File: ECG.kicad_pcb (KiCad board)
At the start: 4 copper layers, 60 x 60 mm, 95 parts, among them J1 SJ-3566AN, J2 Conn_01x02_Male, J3 Conn_01x08_Male, J4 Conn_01x02_Male, J5 Conn_ARM_JTAG_SWD_10, Q1 BC858, Q2 Q_NMOS_DGS, U1 ADR4525, U2 LTC3531, U3 INA333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

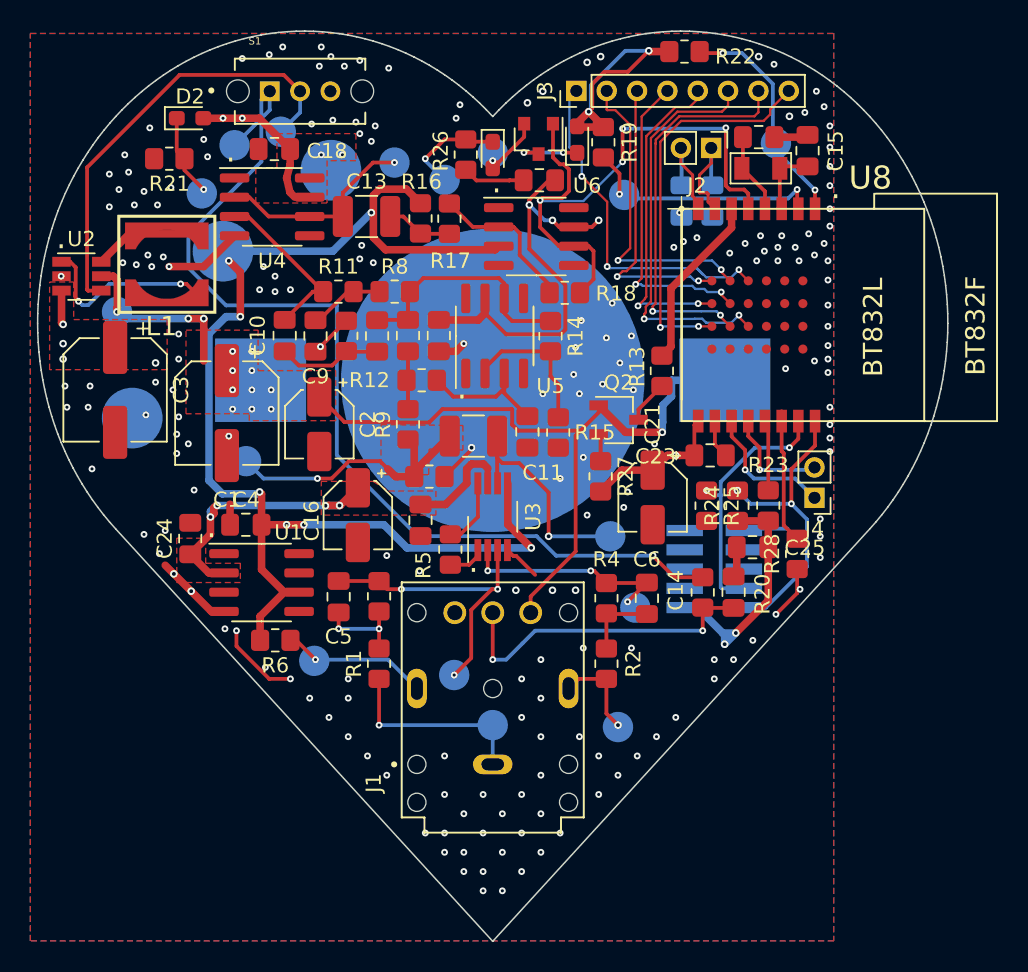
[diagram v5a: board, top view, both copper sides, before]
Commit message: Updated silk screen
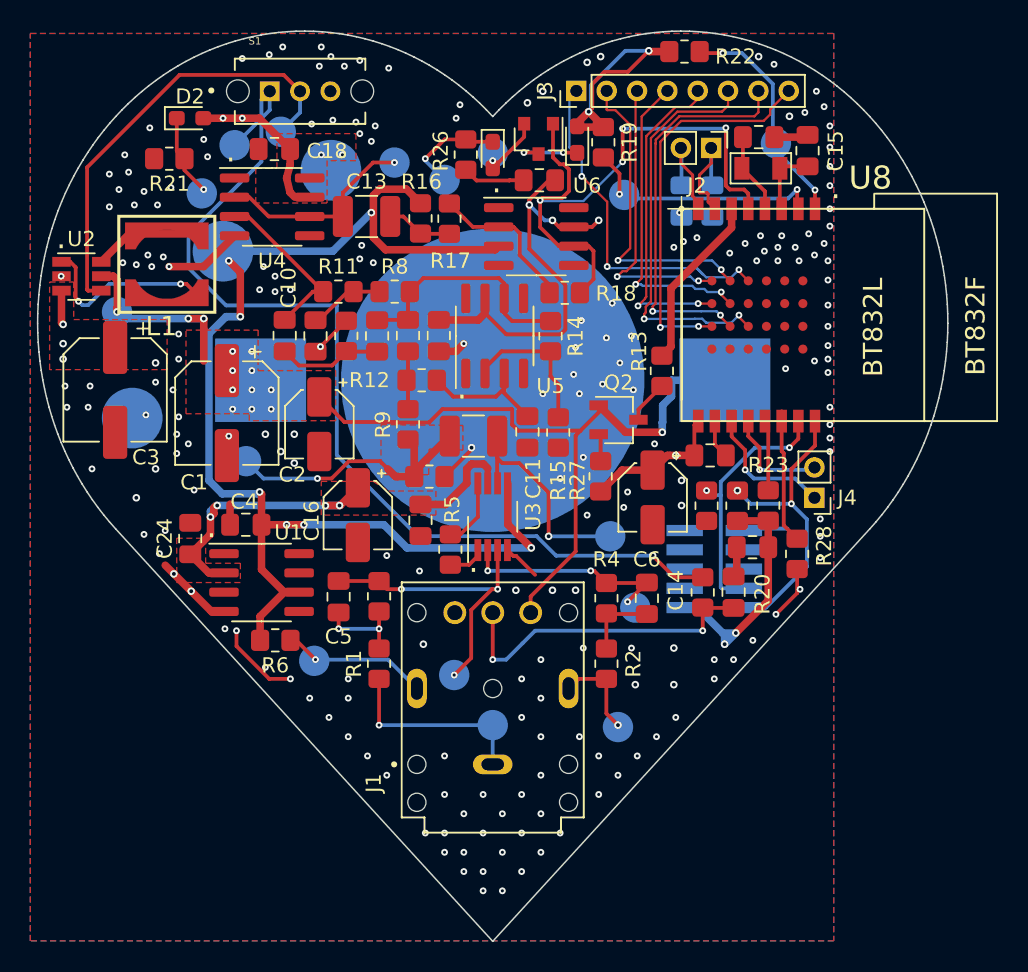
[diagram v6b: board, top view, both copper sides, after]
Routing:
- net GND: vias 188 -> 200
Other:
- board text added: "HealthHub 1.0.1"
- board text removed: "HealthHub 1.0.0"

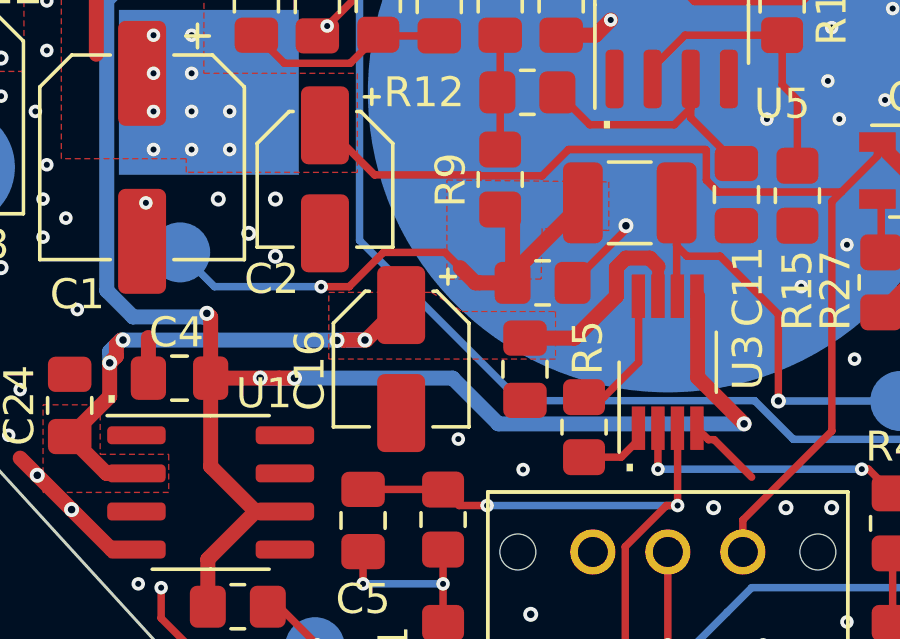
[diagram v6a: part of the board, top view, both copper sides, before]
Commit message: #24 - Updated AC couple
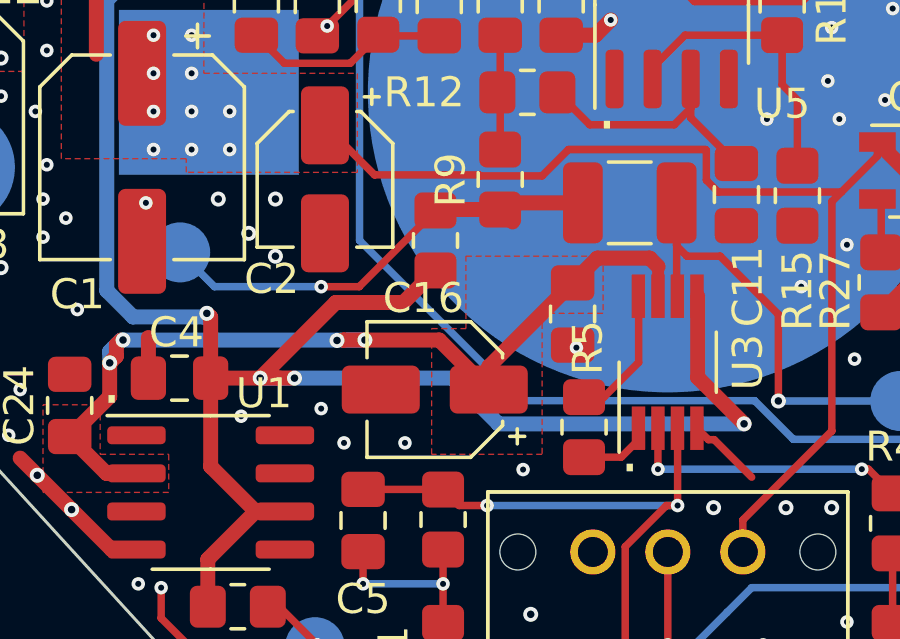
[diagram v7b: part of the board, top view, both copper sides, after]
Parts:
- moved R7 3.84 mm to (144.0, 108.4), turned to 90 degrees
- moved C17 2.43 mm to (148.6, 110.9)
- moved C16 1.51 mm to (144.0, 113.4), turned to 180 degrees
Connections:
- R7 pad 1: /Filters_And_Gain/Vin -> 2.5V
- R7 pad 2: GND -> /Filters_And_Gain/Vin
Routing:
- net 2.5V: track 82.5 -> 89.8 mm
- net 3.3V: track 121.3 -> 126.3 mm
- net /Filters_And_Gain/Vin: track 18.7 -> 15.6 mm
- net GND: track 49.0 -> 46.3 mm, vias 200 -> 203
- removed copper zone on F.Cu, net /Filters_And_Gain/Vin

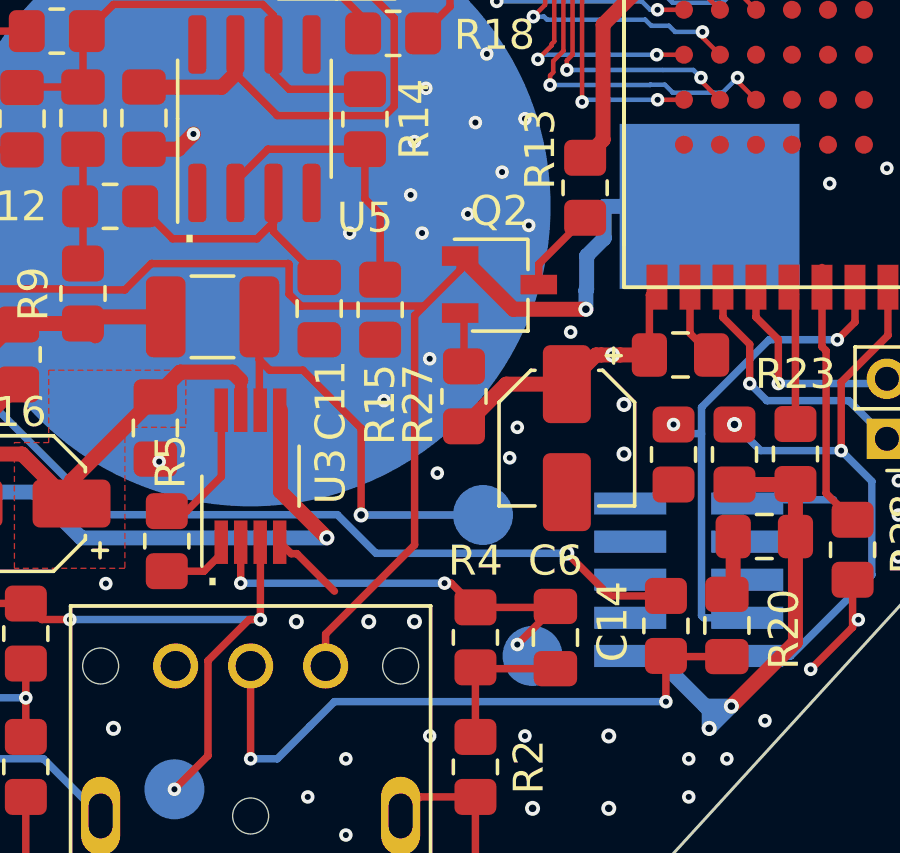
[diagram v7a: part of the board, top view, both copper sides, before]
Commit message: #23 - Add high side power switcher
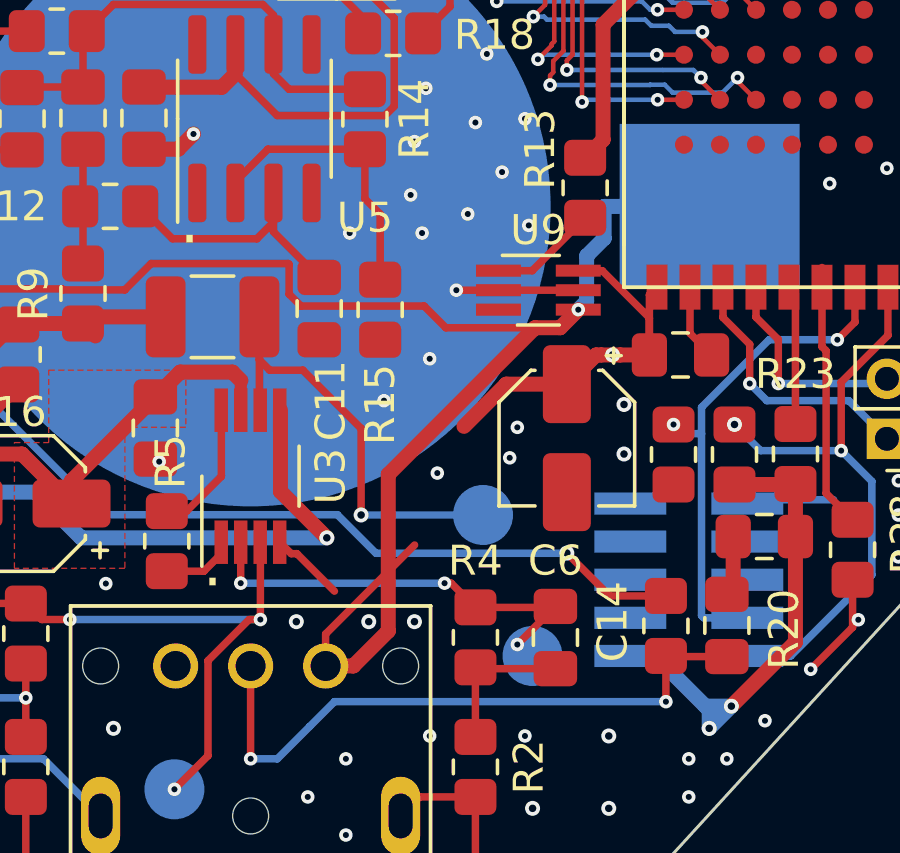
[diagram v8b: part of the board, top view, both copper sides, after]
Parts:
- removed Q2: Q_NMOS_DGS, Package_TO_SOT_SMD:TSOT-23
- removed R27: 100, Resistor_SMD:R_0805_2012Metric_Pad1.20x1.40mm_HandSolder
- added U9: MIC9409, Package_TO_SOT_SMD:SOT-363_SC-70-6_Handsoldering, F.Cu at (161.4, 106.3)
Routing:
- net GND: track 46.3 -> 52.9 mm
- net Vbatt: track 60.1 -> 65.4 mm
- net 3.3V: track 126.3 -> 130.5 mm
- net Net-(Q2-Pad2): track 1.83 -> 0.00 mm
- net Net-(R13-Pad2): track 2.94 -> 3.69 mm
